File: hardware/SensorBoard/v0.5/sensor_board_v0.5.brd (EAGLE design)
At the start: 46.8 x 39.9 mm, 59 parts, among them IC1 MCP1703CB, IC2 MCP1703CB, J3 USB-MICROB, Q1 MMBT5088, U1 ATMEGA328P, U2 TSL2561FN, U4 MPL115A, U5 FT231XS, Y1 16MHZ

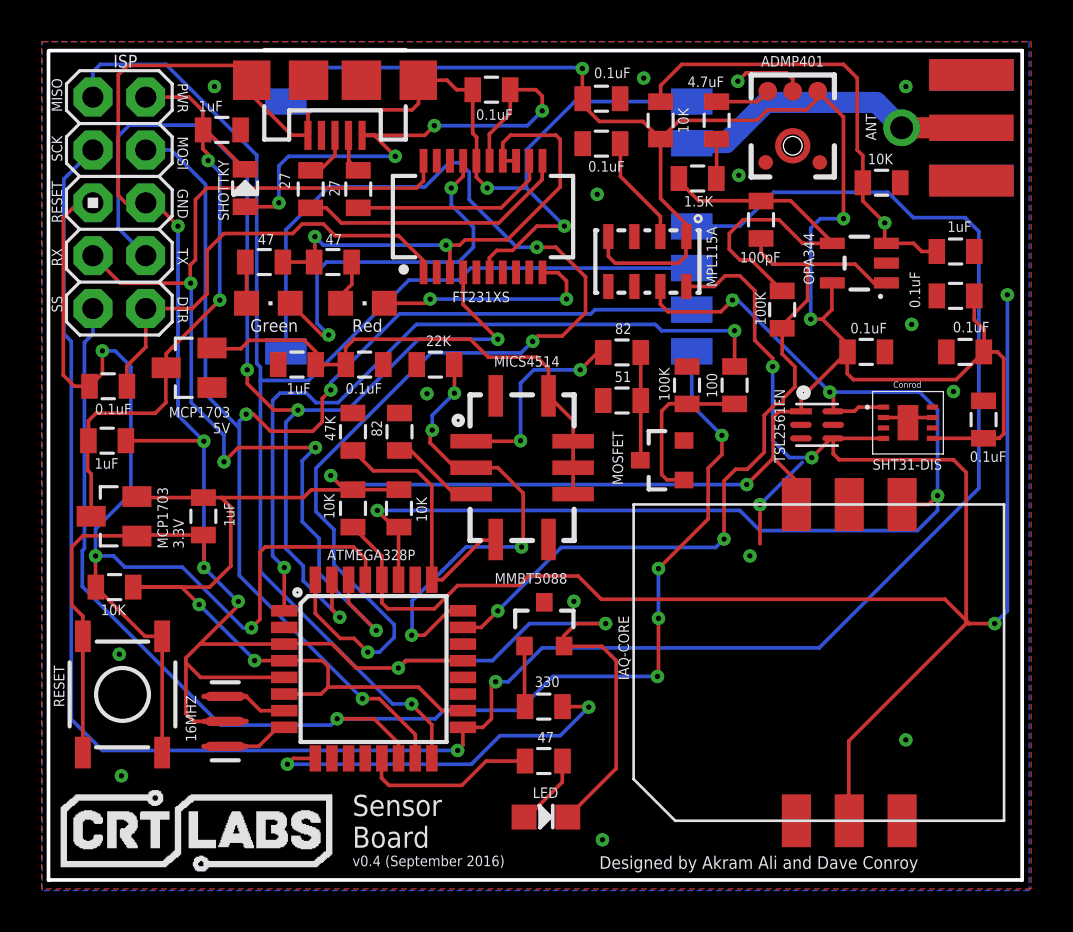
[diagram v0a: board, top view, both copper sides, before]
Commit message: Removed NPN transistor
connected everything to common GND
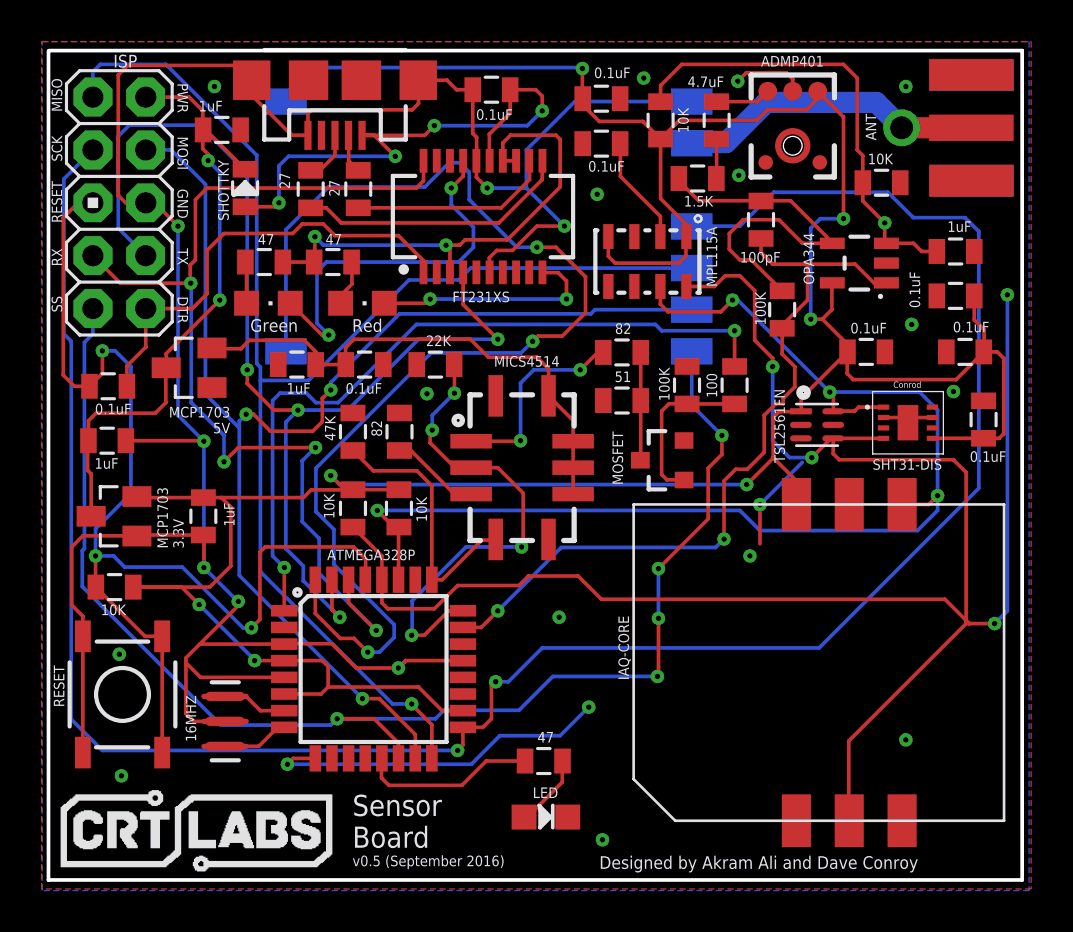
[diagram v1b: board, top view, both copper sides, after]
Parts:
- removed Q1: MMBT5088, SparkFun-DiscreteSemi:SOT23-3
- removed R2: 330, SparkFun-Passives:0805
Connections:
- removed net GND0: C10.2, C13.2, C14.2, C16.2, C17.2, C3.2, C4.2, C5.2, C7.2, C9.2, IAQ-CORE.GND, IC2.1, MOSFET.2, Q1.3, R1.1, R14.1, R15.1, R16.1, R17.1, R19.1, U$1.P$2, U$1.P$7, U$1.P$8, U$1.PAD, U$2.2, U$2.4, U$2.6, U$3.2, U2.3, U4.3, X1.GND@1, X1.GND@2, X1.GND@3, X1.GND@4
- removed net N$1: Q1.1, R2.2
- net D5: no longer R2.1
- net GND: now also C10.2, C13.2, C14.2, C16.2, C17.2, C3.2, C4.2, C5.2, C7.2, C9.2, IAQ-CORE.GND, IC2.1, MOSFET.2, R1.1, R14.1, R15.1, R16.1, R17.1, R19.1, U$1.P$2, U$1.P$7, U$1.P$8, U$1.PAD, U$2.2, U$2.4, U$2.6, U$3.2, U2.3, U4.3, X1.GND@1, X1.GND@2, X1.GND@3, X1.GND@4; no longer Q1.2
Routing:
- net GND: track 150.0 -> 136.1 mm, vias 8 -> 23
- net GND0: track 10.8 -> 0.00 mm, vias 16 -> 0
- net N$1: track 2.94 -> 0.00 mm
- net D5: track 18.3 -> 17.1 mm
- added copper zone on layer 1, net GND
- added copper zone on layer 16, net GND
- removed copper zone on layer 1, net GND0
- removed copper zone on layer 16, net GND0
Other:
- board text added: "v0.5 (September 2016)"
- board text removed: "v0.4 (September 2016)"

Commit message: Increased thickness of power lines to 16
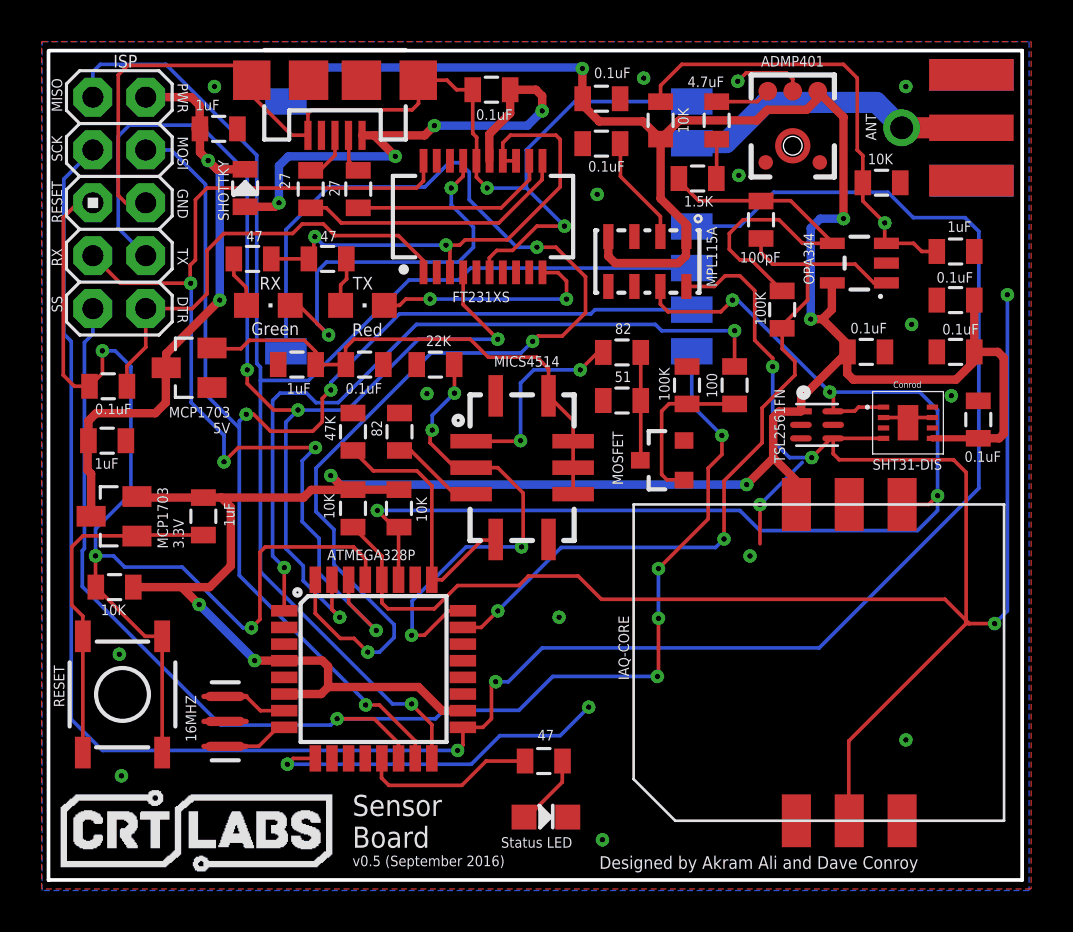
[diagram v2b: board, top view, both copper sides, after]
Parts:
- moved R9 0.58 mm to (15.7, 36.5)
- moved C4 0.46 mm to (49.5, 32.0)
- moved R10 0.30 mm to (19.3, 36.5)
- moved C5 0.25 mm to (50.6, 28.8)
- moved C10 0.20 mm to (49.5, 34.5)
- moved C16 0.16 mm to (14.1, 42.7)
- moved RX 0.10 mm to (16.5, 34.2)
- moved TX 0.10 mm to (21.0, 34.2)
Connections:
- net N$24 renamed VBUS
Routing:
- net GND: track 136.1 -> 81.2 mm, vias 23 -> 18
- net PWR: track 30.0 -> 29.2 mm
- net A0: track 37.5 -> 37.0 mm
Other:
- board text added: "Status LED"
- board text removed: "LED"

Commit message: Added I2C addresses in schematic
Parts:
- renumbered IC1 to U8, IC2 to U9, U$1 to U7, U$2 to U6
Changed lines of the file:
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@@
 <attribute name="NAME" x="33.7886" y="16.2306" size="0.508" layer="121" font="vector" rot="R90"/>
 </element>
-<element name="U$1" library="thomasb9511" package="SHT3X" value="SHT31-DIS" x="47.1932" y="28.6004" smashed="yes">
+<element name="U7" library="thomasb9511" package="SHT3X" value="SHT31-DIS" x="47.1932" y="28.6004" smashed="yes">
 <attribute name="OC_NEWARK" value="47Y1304" x="47.1932" y="28.6004" size="1.778" layer="27" display="off"/>
 <attribute name="MF" value="" x="47.1932" y="28.6004" size="1.778" layer="27" display="off"/>
@@
 <attribute name="VALUE" x="28.5242" y="7.112" size="1.27" layer="27"/>
 </element>
-<element name="IC1" library="linear" package="SOT23" value="MCP1703CB" x="9.0424" y="24.1046" smashed="yes" rot="R90">
+<element name="U8" library="linear" package="SOT23" value="MCP1703CB" x="9.0424" y="24.1046" smashed="yes" rot="R90">
 <attribute name="OC_NEWARK" value="18T9177" x="9.0424" y="24.1046" size="1.778" layer="27" rot="R90" display="off"/>
 <attribute name="MF" value="" x="9.0424" y="24.1046" size="1.778" layer="27" rot="R90" display="off"/>
@@
 <attribute name="VALUE" x="20.1676" y="29.9974" size="0.508" layer="121" font="vector"/>
 </element>
-<element name="IC2" library="linear" package="SOT23" value="MCP1703CB" x="12.6492" y="31.242" smashed="yes" rot="R90">
+<element name="U9" library="linear" package="SOT23" value="MCP1703CB" x="12.6492" y="31.242" smashed="yes" rot="R90">
 <attribute name="MF" value="" x="12.6492" y="31.242" size="1.778" layer="27" rot="R90" display="off"/>
 <attribute name="MPN" value="MCP1703T-2502E/CB" x="12.6492" y="31.242" size="1.778" layer="27" rot="R90" display="off"/>
@@
 <attribute name="VALUE" x="18.4912" y="30.5054" size="0.508" layer="121" font="vector" rot="R180"/>
 </element>
-<element name="U$2" library="SparkFun-Sensors" package="ADMP401" value="ADMP401" x="41.656" y="41.91" smashed="yes">
+<element name="U6" library="SparkFun-Sensors" package="ADMP401" value="ADMP401" x="41.656" y="41.91" smashed="yes">
 <attribute name="VALUE" x="40.1292" y="45.7172" size="0.508" layer="121" font="vector"/>
 </element>
@@
 <contactref element="Y1" pad="2"/>
 <contactref element="C1" pad="2"/>
-<contactref element="IC1" pad="1"/>
+<contactref element="U8" pad="1"/>
 <contactref element="C6" pad="2"/>
 <contactref element="RESET" pad="1"/>
@@
 <contactref element="C7" pad="2"/>
 <contactref element="C16" pad="2"/>
-<contactref element="IC2" pad="1"/>
+<contactref element="U9" pad="1"/>
 <contactref element="C17" pad="2"/>
-<contactref element="U$2" pad="2"/>
-<contactref element="U$2" pad="4"/>
-<contactref element="U$2" pad="6"/>
+<contactref element="U6" pad="2"/>
+<contactref element="U6" pad="4"/>
+<contactref element="U6" pad="6"/>
 <contactref element="C10" pad="2"/>
 <via x="39.0144" y="45.0088" extent="1-16" drill="0.254" diameter="0.127"/>
@@
 <contactref element="U$3" pad="2"/>
 <contactref element="C4" pad="2"/>
-<contactref element="U$1" pad="P$8"/>
-<contactref element="U$1" pad="PAD"/>
-<contactref element="U$1" pad="P$7"/>
+<contactref element="U7" pad="P$8"/>
+<contactref element="U7" pad="PAD"/>
+<contactref element="U7" pad="P$7"/>
 <wire x1="48.3682" y1="28.8504" x2="47.4432" y2="28.8504" width="0.1778" layer="1"/>
 <wire x1="47.4432" y1="28.8504" x2="47.1932" y2="28.6004" width="0.1778" layer="1"/>
-<contactref element="U$1" pad="P$2"/>
+<contactref element="U7" pad="P$2"/>
 <wire x1="46.0182" y1="28.8504" x2="46.9432" y2="28.8504" width="0.1778" layer="1"/>
 <via x="32.512" y="8.5598" extent="1-16" drill="0.254" diameter="0.127"/>
@@
 <contactref element="C3" pad="1"/>
 <contactref element="C5" pad="1"/>
-<contactref element="U$1" pad="P$5"/>
+<contactref element="U7" pad="P$5"/>
 <contactref element="C4" pad="1"/>
-<contactref element="IC1" pad="2"/>
+<contactref element="U8" pad="2"/>
 <contactref element="C6" pad="1"/>
 <contactref element="R13" pad="2"/>
@@
 <contactref element="R7" pad="2"/>
 <contactref element="U$3" pad="5"/>
-<contactref element="U$2" pad="5"/>
+<contactref element="U6" pad="5"/>
 <contactref element="C10" pad="1"/>
 <via x="42.5196" y="33.5788" extent="1-16" drill="0.254" diameter="0.127"/>
@@
 <contactref element="U1" pad="28"/>
 <contactref element="IAQ-CORE" pad="SCL"/>
-<contactref element="U$1" pad="P$4"/>
+<contactref element="U7" pad="P$4"/>
 <contactref element="R6" pad="1"/>
 <contactref element="U2" pad="4"/>
@@
 <signal name="SDA">
 <contactref element="U1" pad="27"/>
-<contactref element="U$1" pad="P$1"/>
+<contactref element="U7" pad="P$1"/>
 <contactref element="R5" pad="1"/>
 <contactref element="IAQ-CORE" pad="SDA"/>
@@
 </signal>
 <signal name="PWR">
-<contactref element="IC1" pad="3"/>
+<contactref element="U8" pad="3"/>
 <contactref element="C1" pad="1"/>
 <contactref element="J2" pad="2"/>
-<contactref element="IC2" pad="3"/>
+<contactref element="U9" pad="3"/>
 <contactref element="C16" pad="1"/>
 <contactref element="R11" pad="1"/>
@@
 <wire x1="29.3624" y1="31.75" x2="27.0256" y2="31.75" width="0.1778" layer="1"/>
 <contactref element="C7" pad="1"/>
-<contactref element="IC2" pad="2"/>
+<contactref element="U9" pad="2"/>
 <contactref element="C17" pad="1"/>
 <wire x1="27.0256" y1="31.75" x2="26.162" y2="32.6136" width="0.1778" layer="1"/>
@@
 </signal>
 <signal name="N$7">
-<contactref element="U$2" pad="1"/>
+<contactref element="U6" pad="1"/>
 <contactref element="C8" pad="1"/>
 <wire x1="37.9984" y1="44.0292" x2="39.9552" y2="44.0292" width="0.1778" layer="1"/>
